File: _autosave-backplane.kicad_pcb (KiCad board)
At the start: 4 copper layers, 110 x 90 mm, 45 parts, among them IC1 SiC437AED-T1-GE3, J1 46010-0622, J2 46010-0622, J4 212520-1006, J5 XT60PW-F

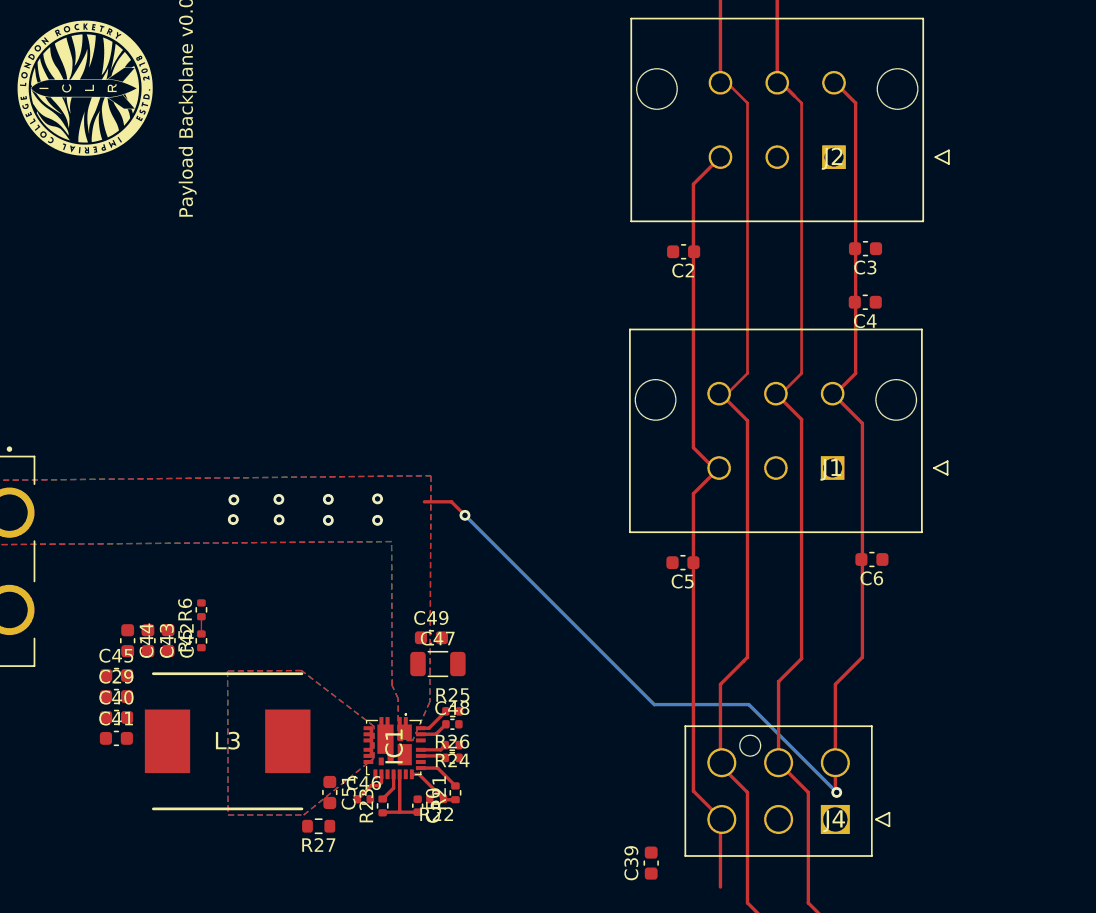
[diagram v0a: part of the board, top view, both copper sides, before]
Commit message: neatened things
leds
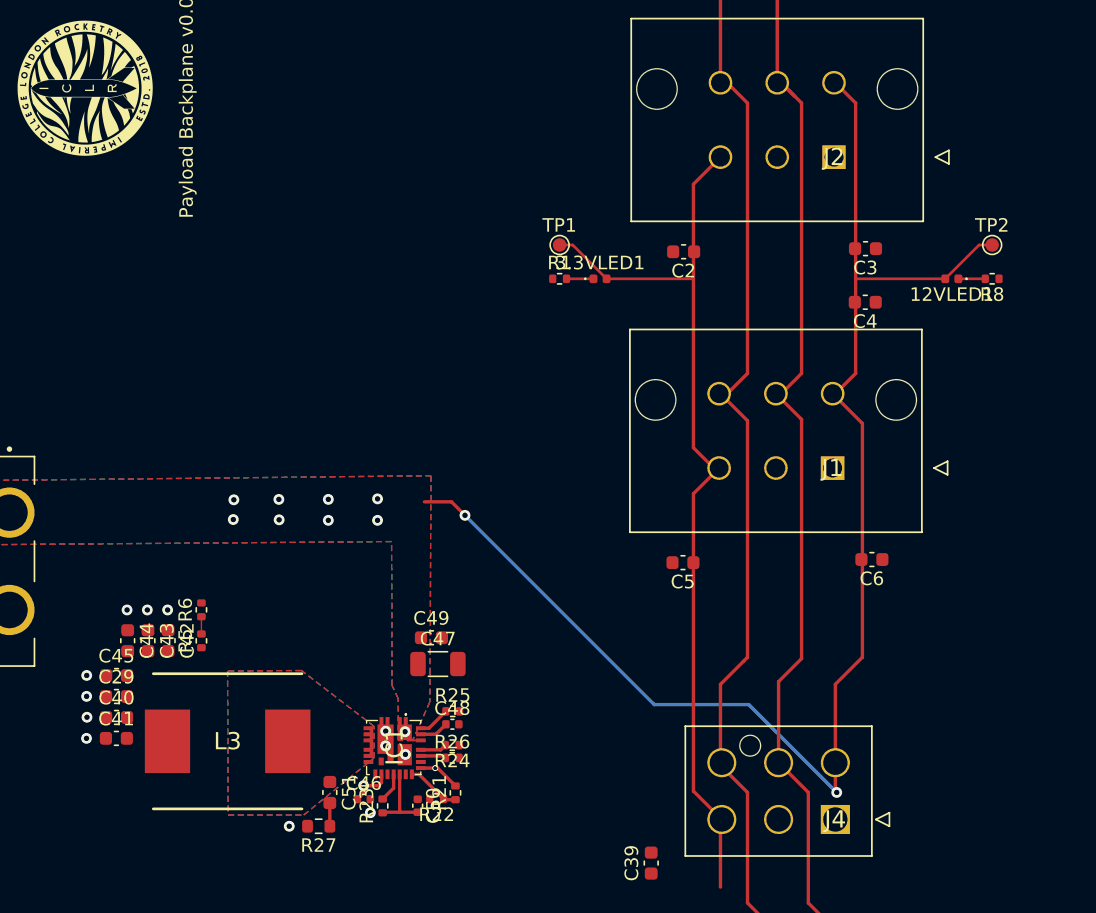
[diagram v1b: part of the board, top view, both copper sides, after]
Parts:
- added 12VLED1: 12VLED, LED_SMD:LED_0402_1005Metric, F.Cu at (160.0, 90.0)
- added 3.3VLED1: 3.3VLED, LED_SMD:LED_0402_1005Metric, F.Cu at (134.0, 90.0)
- added R1: 1k, Resistor_SMD:R_0402_1005Metric, F.Cu at (131.0, 90.0)
- added R8: 1k, Resistor_SMD:R_0402_1005Metric, F.Cu at (163.0, 90.0)
- added TP1: TestPoint, TestPoint:TestPoint_Pad_D1.0mm, F.Cu at (131.0, 87.5)
- added TP2: TestPoint, TestPoint:TestPoint_Pad_D1.0mm, F.Cu at (163.0, 87.5)
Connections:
- J5 pad 2: /GND -> GND
- J5 pad S1: /GND -> GND
- J5 pad S2: /GND -> GND
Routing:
- net +12V: track 95.5 -> 106.6 mm
- net +3.3V: track 57.4 -> 68.3 mm
- net Net-(3.3VLED1-K): track 0.00 -> 2.00 mm
- net Net-(12VLED1-K): track 0.00 -> 1.99 mm
- net Net-(C51-Pad2): track 0.00 -> 1.72 mm
- net Net-(IC1-EN): track 0.00 -> 1.59 mm, vias 0 -> 1
- net Net-(IC1-V_DRV): track 2.90 -> 3.22 mm, vias 0 -> 1
- net RBUS_uC_V: vias 0 -> 1
- net GND: vias 70 -> 82
